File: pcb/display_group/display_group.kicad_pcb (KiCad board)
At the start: 2 copper layers, 81.3 x 25 mm, 10 parts, among them J1 L, J16 R, J17 L, J18 R, J2 R, J3 SELECT, J4 SEGMENTS, J5 L, J6 R, J7 L

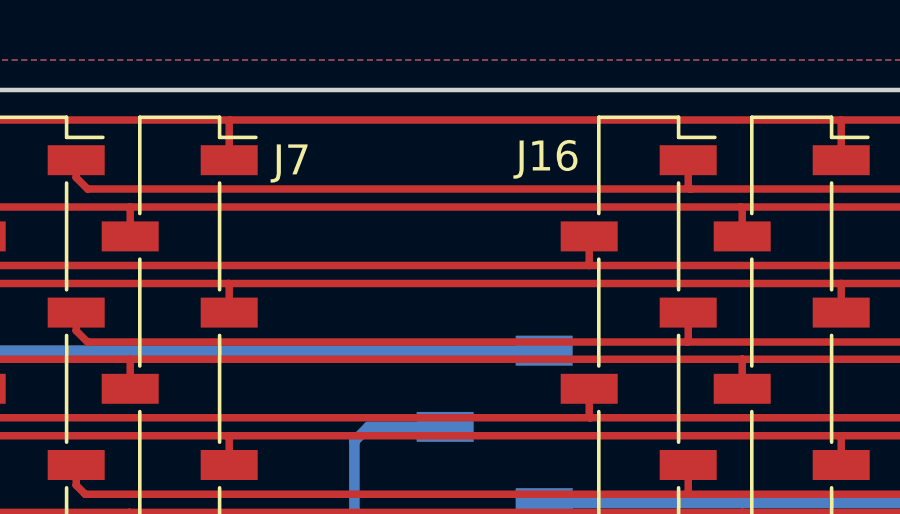
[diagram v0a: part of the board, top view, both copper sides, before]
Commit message: added name embossing to the display_group board
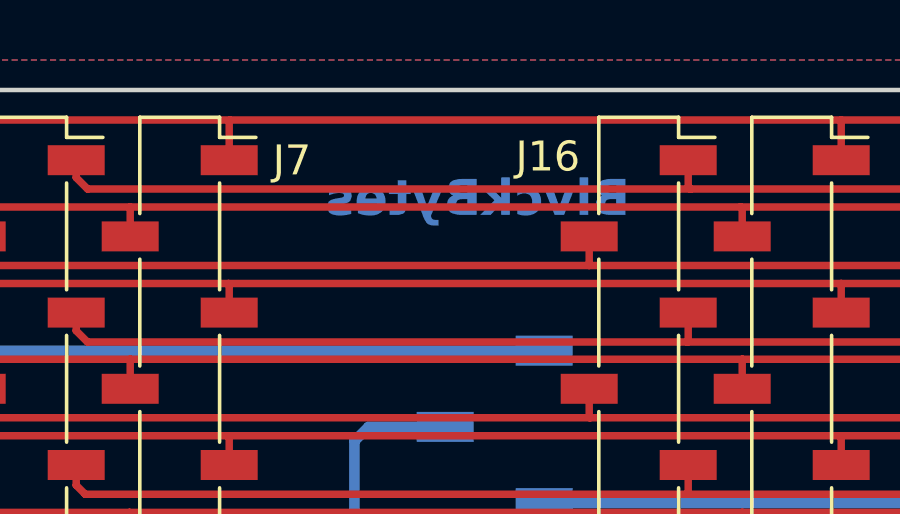
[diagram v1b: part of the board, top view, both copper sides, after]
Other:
- board text added: "BlvckBytes"
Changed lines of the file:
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@@
   (gr_rect (start 0 0) (end 15.24 22.97)
     (stroke (width 0.15) (type default)) (fill none) (layer "User.1"))
+  (gr_text "BlvckBytes" (at 115.81 132.31) (layer "B.Cu" knockout)
+    (effects (font (size 1.2 1.2) (thickness 0.25) bold) (justify left bottom mirror))
+  )
   (dimension (type orthogonal) (layer "User.1")
     (pts (xy 100.8 140.5) (xy 116.1 140.5))
